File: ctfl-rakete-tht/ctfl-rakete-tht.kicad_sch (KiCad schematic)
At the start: 32 parts, among them J1 Conn_02x03_Odd_Even, SW1 SW_SPDT, U1 ATtiny212-SS

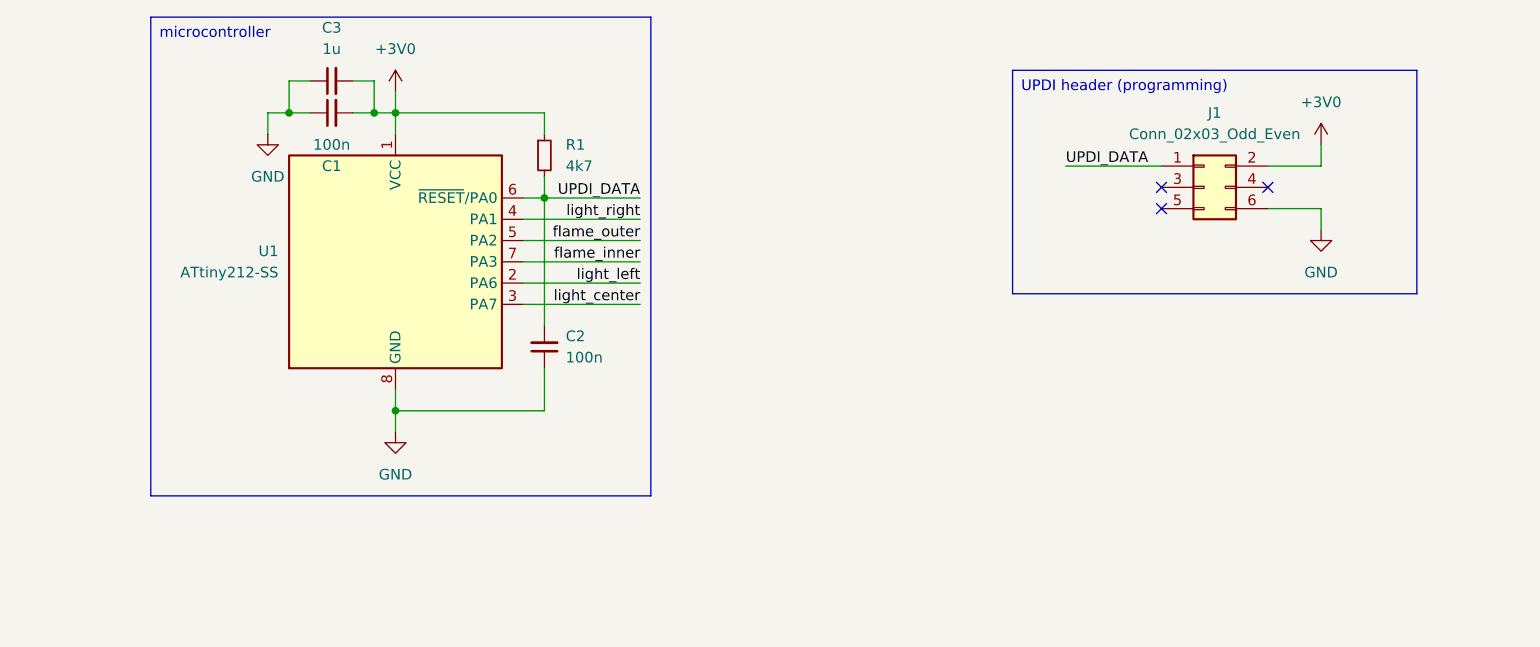
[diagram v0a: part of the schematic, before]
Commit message: WIP: started work on changing the programming header footprint to a more suitable 3 pin variant
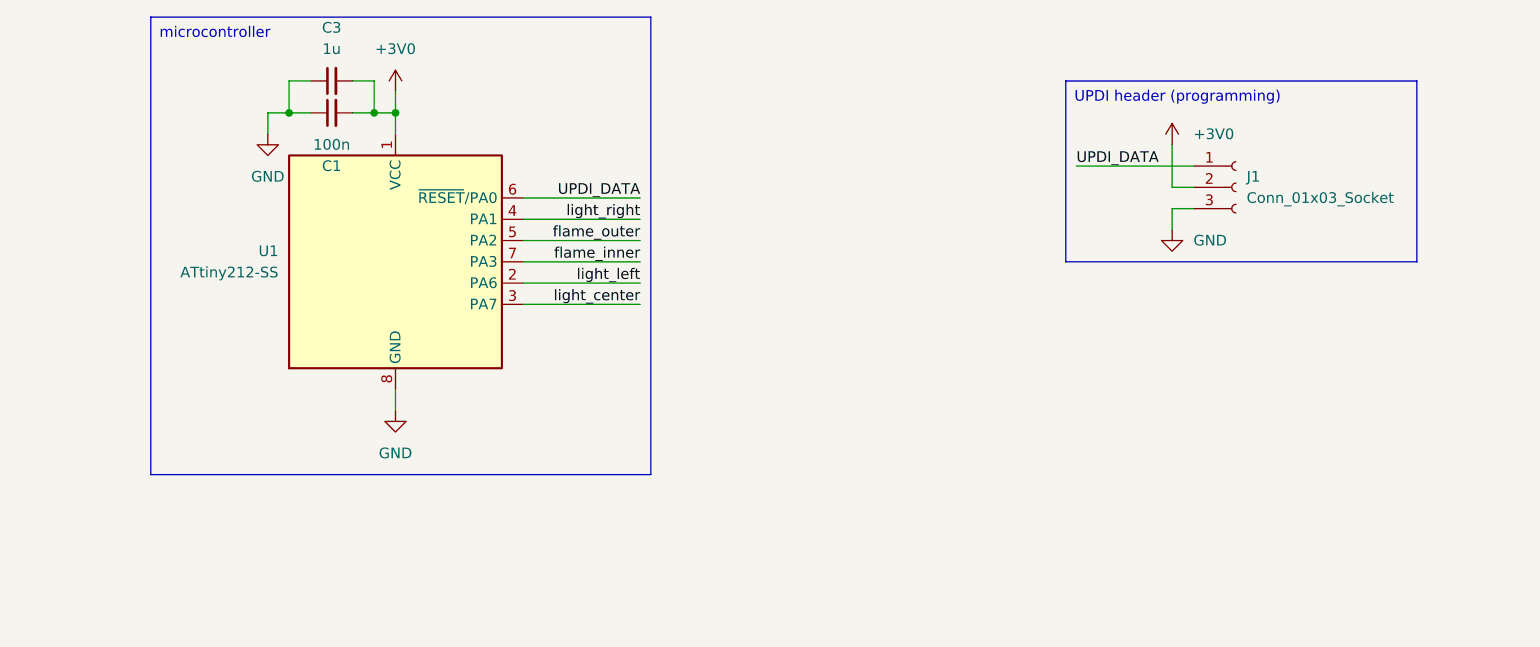
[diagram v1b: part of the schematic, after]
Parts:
- removed C2: 100n, Capacitor_SMD:C_0805_2012Metric_Pad1.18x1.45mm_HandSolder, symbol Device:C_Small
- removed J1: Conn_02x03_Odd_Even, Connector_PinHeader_2.54mm:PinHeader_2x03_P2.54mm_Vertical_SMD, symbol Connector_Generic:Conn_02x03_Odd_Even
- removed R1: 4k7, Resistor_SMD:R_0805_2012Metric_Pad1.20x1.40mm_HandSolder, symbol Device:R_Small
- added J1: Conn_01x03_Socket, symbol Connector:Conn_01x03_Socket
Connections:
- net +3V0: now also J1.2 (Pin_2)
- net GND: now also J1.3 (Pin_3)
- net UPDI_DATA: now also J1.1 (Pin_1)
- no-connect marks 8 -> 5

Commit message: close #3: replaced old programming header with a 1x3 horizontal SMD pin socket footprint (don't let the 3D model of it fool you)
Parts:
- J1: footprint (none) -> local:PinSocket_1x03_P2.54mm_Horizontal_SMD
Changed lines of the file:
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@@
 			)
 		)
-		(property "Footprint" ""
+		(property "Footprint" "local:PinSocket_1x03_P2.54mm_Horizontal_SMD"
 			(at 240.03 39.37 0)
 			(effects
